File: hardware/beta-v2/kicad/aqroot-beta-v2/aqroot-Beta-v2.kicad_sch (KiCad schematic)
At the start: 0 parts

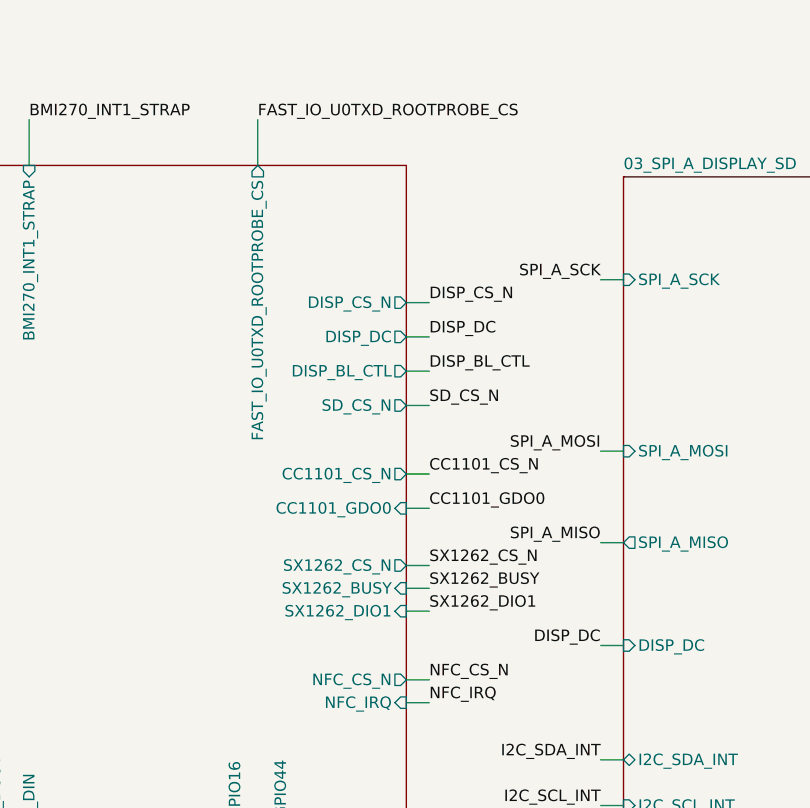
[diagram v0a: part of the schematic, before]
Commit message: hardware: migrate Full Beta v2 MCU core (FBV2-S1-002)
Closes the two power-tree values the CTO ruled on and migrates 02_MCU_CORE.
Task gate FBV2-S1-MCU-CORE = PASS. FBV2-S1 itself is 2 of 9 sheets.

P-20 - R95 680R -> 560R. Recovery recomputed from the captured circuit:
8.36 mA nominal at VBUS 5.0 V into a 0 V pack, 7.93-8.80 mA across 4.75-5.25 V,
back inside the accepted 5-10 mA band that B-26 is measured against.

The recomputation also showed that 680R was NOT arbitrary:
(5.00 - 0.32 + 4.2) / 680 = 13.06 mA is exactly B-27's recorded ~13 mA
single-fault ceiling. With 560R that ceiling becomes ~15.9 mA nominal and
~16.6 mA worst case - 0.0066 C on a 2500 mAh pack, still bounded by R95, still
unidirectional through D12, still self-annunciating. B-27 is amended in place
rather than left reading a number that is no longer true. The trade is explicit:
~21% more recovery current for ~22% more single-fault current.

P-21 - the OV trip is derived, not typed. The datasheet threshold was fetched
first (LTC4368, Farnell mirror 2243878): V_OV 492.5 / 500 / 507.5 mV rising,
hysteresis 20 / 25 / 32 mV, UV/OV leakage 10 nA max, "Adjustable +/-1.5%".
R77 4.02M -> 3.65M 1%, R78 unchanged at 442k:
0.500 x (3.65M + 442k) / 442k = 4.629 V.
Nominal 4.63 V; 4.48-4.78 V over comparator and 1% resistor tolerance;
4.44-4.82 V including worst-case OV pin leakage; release 4.40 V nominal.
Above a 4.35 V-class pack with 129 mV of worst-case margin, 420 mV below the
5.05 V first capture, and no lockout hazard because release sits above float.
3.65M is already R91's value, so this REMOVES a BOM line.

02_MCU_CORE migrated:

- GPIO38 = NATIVE_A and GPIO47 = NATIVE_B, both hierarchical and bidirectional.
  SX1262_DIO1 no longer reaches the MCU at all; under D-089 it terminates on the
  internal expander U2, which is sheet 08.
- GPIO46 = DISP_BL_CTL. GPIO46 is a strapping pin that MUST read LOW at reset -
  GPIO0 = 0 alone does not select Joint Download Boot, GPIO46 = 0 is also
  required. Three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
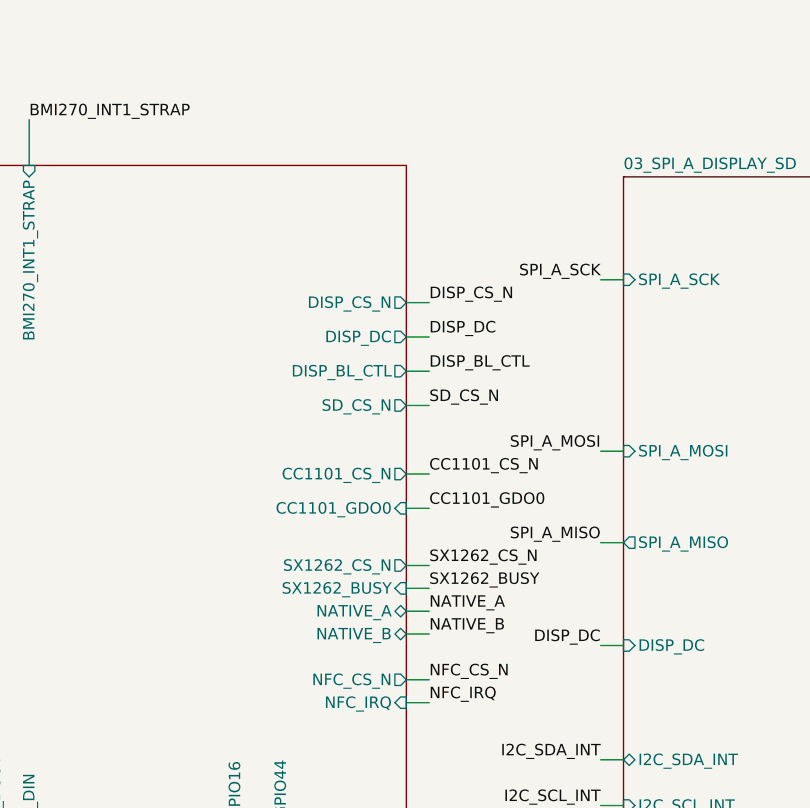
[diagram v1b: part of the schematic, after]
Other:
- sheet 02_MCU_CORE ports: added NATIVE_A, NATIVE_B; removed FAST_IO_U0TXD_ROOTPROBE_CS, SX1262_DIO1
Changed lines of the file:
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@@
 	(wire
 		(pts
-			(xy 185.42 25.4) (xy 185.42 20.32)
-		)
-		(stroke
-			(width 0)
-			(type default)
-		)
-	)
-	(wire
-		(pts
 			(xy 388.62 152.4) (xy 391.16 152.4)
 		)
@@
 	(wire
 		(pts
-			(xy 201.93 74.93) (xy 204.47 74.93)
-		)
-		(stroke
-			(width 0)
-			(type default)
-		)
-	)
-	(wire
-		(pts
 			(xy 133.35 245.11) (xy 135.89 245.11)
 		)
@@
 		)
 	)
-	(label "SX1262_DIO1"
-		(at 204.47 74.93 0)
-		(effects
-			(font
-				(size 1.27 1.27)
-			)
-			(justify left bottom)
-		)
-	)
 	(label "XGPIO0"
 		(at 391.16 132.08 0)
@@
 		)
 	)
-	(label "FAST_IO_U0TXD_ROOTPROBE_CS"
-		(at 185.42 20.32 0)
-		(effects
-			(font
-				(size 1.27 1.27)
-			)
-			(justify left bottom)
-		)
-	)
 	(label "I2C_SDA_INT"
 		(at 52.07 228.6 180)
@@
 			)
 		)
-		(pin "FAST_IO_U0TXD_ROOTPROBE_CS" output
-			(at 185.42 25.4 90)
-			(effects
-				(font
-					(size 1.27 1.27)
-				)
-				(justify right)
-			)
-		)
 		(pin "I2C_SCL_INT" output
 			(at 129.54 46.99 180)
@@
 			)
 		)
-		(pin "SX1262_DIO1" input
+		(pin "NATIVE_A" bidirectional
 			(at 201.93 74.93 0)
 			(effects
@@
 			)
 		)
+		(pin "NATIVE_B" bidirectional
+			(at 201.93 77.47 0)
+			(effects
+				(font
+					(size 1.27 1.27)
+				)
+				(justify right)
+			)
+		)
 		(pin "USB_D_MCU_N" bidirectional
 			(at 144.78 25.4 90)
@@
 		(effects
 			(font
+				(size 1.27 1.27)
+			)
+			(justify left bottom)
+		)
+	)
+	(wire
+		(pts
+			(xy 201.93 74.93) (xy 204.47 74.93)
+		)
+		(stroke
+			(width 0)
+			(type default)
+		)
+	)
+	(label "NATIVE_A"
+		(at 204.47 74.93 0)
+		(effects
+			(font
+				(size 1.27 1.27)
+			)
+			(justify left bottom)
+		)
+	)
+	(wire
+		(pts
+			(xy 201.93 77.47) (xy 204.47 77.47)
+		)
+		(stroke
+			(width 0)
+			(type default)
+		)
+	)
+	(label "NATIVE_B"
+		(at 204.47 77.47 0)
+		(effects
+			(font

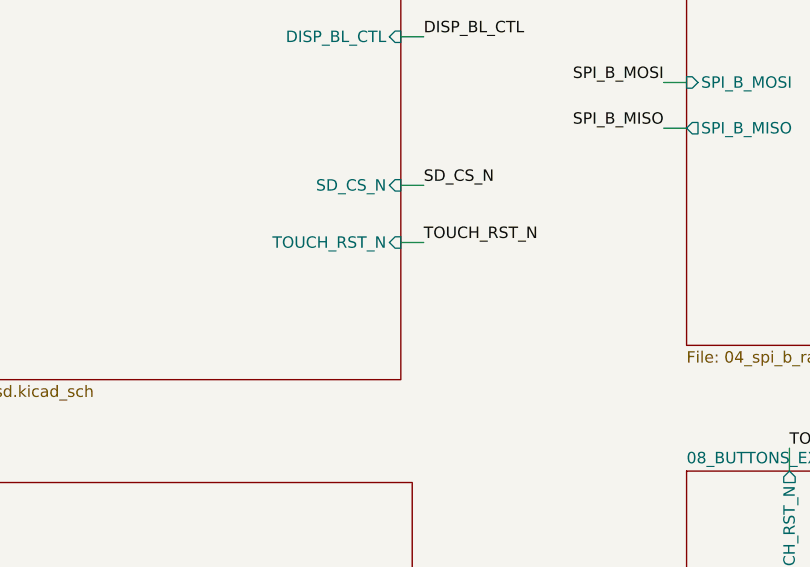
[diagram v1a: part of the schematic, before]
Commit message: hardware: migrate Full Beta v2 display and microSD (FBV2-S1-003)
Fits R111 per CTO ruling and migrates 03_SPI_A_DISPLAY_SD. Task gate
FBV2-S1-DISPLAY-SD = PASS. FBV2-S1 itself is 3 of 9 sheets.

THE INHERITED J1 WOULD HAVE PRODUCED A DEAD DISPLAY, TWICE OVER.

J1 still used the 2.8-inch CH280QV10_CT_50P pin table while its Value and
Footprint fields already read FH69-50S-0.5SH. Pin count matched, connector
matched, ERC was silent. The pin FUNCTIONS did not match ER-TFT035IPS-6:

  panel pin 1/2/3   old: LEDK / LED-A1 / LED-A2   new: LEDA / LEDK / LEDK
                    -> backlight reverse-biased, no light
  panel pin 36/37   old: WR_RS->DISP_DC / RS_SCL->SPI_A_SCK
                    new: WRX(SCL) / D-CX
                    -> clock and D/C swapped, no valid command ever reaches
                       the panel
  panel pin 4,5,6   old: LED-A3, LED-A4, IM0(grounded)   new: NC
  panel pin 7,8,9   old: IM1,IM2,IM3   new: IM0,IM1,IM2  (all three were
                    already +3V3, so 1 1 1 was correct by luck)
  panel pin 46      CTP IRQ, not represented at all

Neither fault is visible from a pin count, a connector MPN or an ERC run. A new
project-library symbol ER-TFT035IPS-6_50P was authored with the vendor table
verbatim (datasheet Rev 2.0 sec 4.1), deliberately keeping the old pin geometry
so the migration is a pin-function change and not a redraw. CH280QV10_CT_50P
stays in the library - Beta-DM still uses it - and is dropped from sheet 03's
symbol cache.

R111 FITTED (D-111). 10k, GPIO45_VDDSPI_STRAP -> GND. VDD_SPI is held LOW
deterministically instead of relying on the chip's internal pull-down alone.
TP1 retained, no capacitance on the net, no peripheral on GPIO45.

B-43 CLOSED WITH A PRIMARY SOURCE (D-116). TPS61169 datasheet SNVSA40B:
R_PD, CTRL pin internal pull-down resistor, 300 kohm, with V_H/V_L = 1.2/0.4 V
and t_SD = 2.5 ms. CTRL's only internal element pulls DOWN, so there is no
mechanism by which the backlight driver can raise the GPIO46 strap. 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
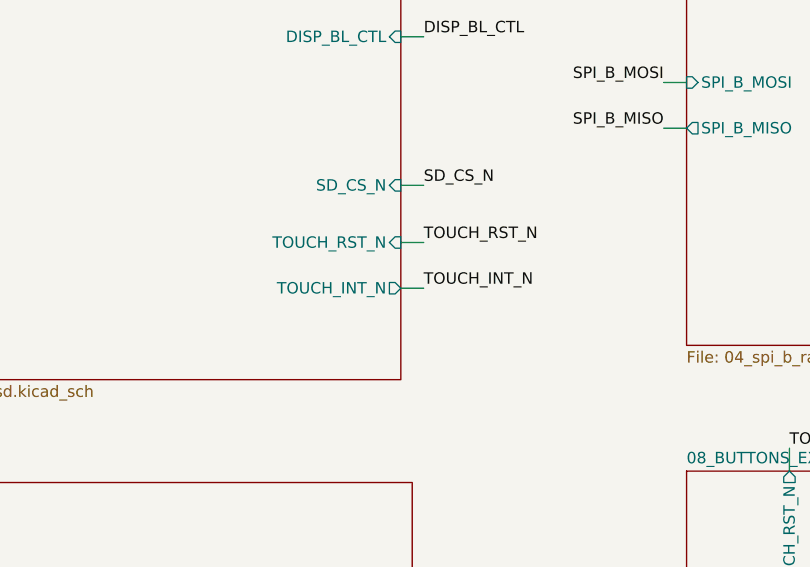
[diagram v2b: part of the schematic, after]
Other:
- sheet 03_SPI_A_DISPLAY_SD ports: added TOUCH_INT_N; removed none
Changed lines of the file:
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@@
+			)
+		)
+		(pin "TOUCH_INT_N" output
+			(at 290.83 95.25 0)
+			(effects
+				(font
+					(size 1.27 1.27)
+				)
+				(justify right)
 			)
 		)
@@
 		(effects
 			(font
+				(size 1.27 1.27)
+			)
+			(justify left bottom)
+		)
+	)
+	(wire
+		(pts
+			(xy 290.83 95.25) (xy 293.37 95.25)
+		)
+		(stroke
+			(width 0)
+			(type default)
+		)
+	)
+	(label "TOUCH_INT_N"
+		(at 293.37 95.25 0)
+		(effects
+			(font

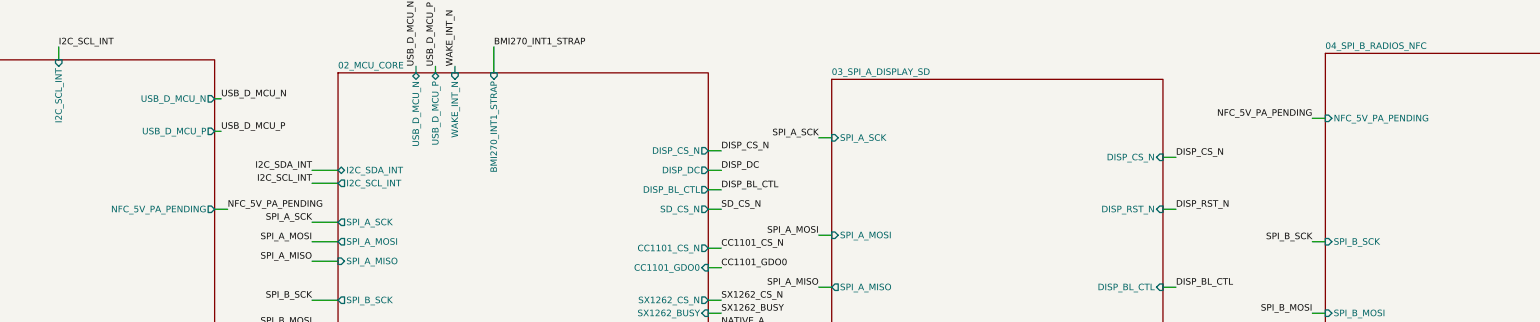
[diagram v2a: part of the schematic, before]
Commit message: hardware: migrate Full Beta v2 radios and NFC (FBV2-S1-004)
Sheet 04. Task gate FBV2-S1-RADIOS-NFC = PASS. FBV2-S1 itself is 4 of 9 sheets.

ERC: 4 errors -> 2. Total 86 -> 68. Zero added, eighteen removed. This is the
first migration task to REDUCE the project's error count, and it did so by
deleting placeholder architecture rather than by suppressing anything.

ZERO *_TBD NETS REMAIN ANYWHERE IN THE PROJECT. Sheet 04 alone retired fourteen.

RF ARCHITECTURE LOCKED (D-118).
433 MHz: INTERNAL flex. U7 IPEX -> 100 mm coax -> Taoglas FXP450.07.0100C against
a plastic wall. 915 MHz: EXTERNAL. U8 IPEX -> short pigtail -> top-panel SMA
female bulkhead, user-changeable. Neither band has a motherboard 50 ohm RF trace,
a matching network, an RF switch or a diplexer - both modules present their own
matched 50 ohm port, so the board's RF involvement at 433/915 is zero copper.
This supersedes the internal-FXP890 plan for 915 in "12 - RF and Antenna Plan".
The U7 IPEX socket must remain SERVICE-ACCESSIBLE with the shell open: if
internal 433 performance disappoints on the first units the flex unplugs and an
external pigtail replaces it with no PCB respin. That is an FBV2-P1 placement
constraint and the reason an internal antenna is an acceptable first-build risk.

433 ANTENNA VERIFIED, MATING PROVEN RATHER THAN ASSUMED (D-119). Taoglas
datasheet SPE-23-8-180-A, verbatim: "410-470MHz Flexible PCB Antenna with 100mm
1.37 IPEX MHFI". 47 x 17 x 0.28 mm, adhesive mount, gain -0.36 / -1.57 /
-0.05 dBi, Active, 54 in stock, $5.52 @ 1, MOQ 1. The antenna terminates in IPEX
MHF I and Ebyte's manual lists the E07-400M10S interface as IPEX-1 / stamp hole;
MHF I, IPEX-1 and U.FL are one mating interface, so no cable variant is needed.
Mechanical reservation recorded for FBV2-P1: plastic wall, LEFT/LOWER-SIDE, NOT
on the PCB, clear of the LiPo, the NFC loop and ferrite, the speaker magnet,
large ground pours, metal bosses, the USB shell, the 915 bulkhead/pigtail and the
IR structures.

915 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
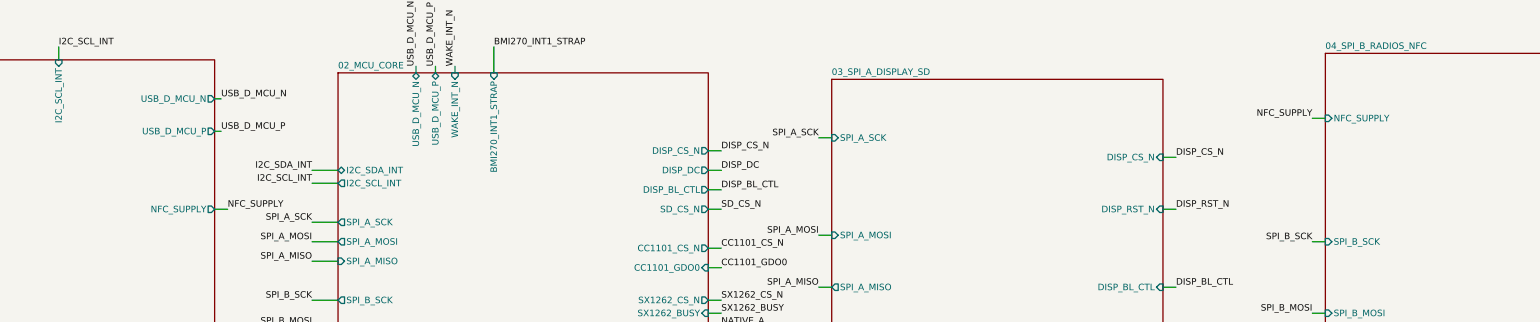
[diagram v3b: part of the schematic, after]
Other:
- sheet 01_POWER_TREE ports: added NFC_SUPPLY; removed NFC_5V_PA_PENDING
- sheet 04_SPI_B_RADIOS_NFC ports: added NFC_SUPPLY; removed NFC_5V_PA_PENDING
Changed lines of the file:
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@@
 		)
 	)
-	(label "NFC_5V_PA_PENDING"
+	(label "NFC_SUPPLY"
 		(at 107.95 52.07 0)
 		(effects
@@
 		)
 	)
-	(label "NFC_5V_PA_PENDING"
+	(label "NFC_SUPPLY"
 		(at 320.04 34.29 180)
 		(effects
@@
 			)
 		)
-		(pin "NFC_5V_PA_PENDING" input
+		(pin "NFC_SUPPLY" input
 			(at 322.58 34.29 180)
 			(effects
@@
 			)
 		)
-		(pin "NFC_5V_PA_PENDING" output
+		(pin "NFC_SUPPLY" output
 			(at 105.41 52.07 0)
 			(effects

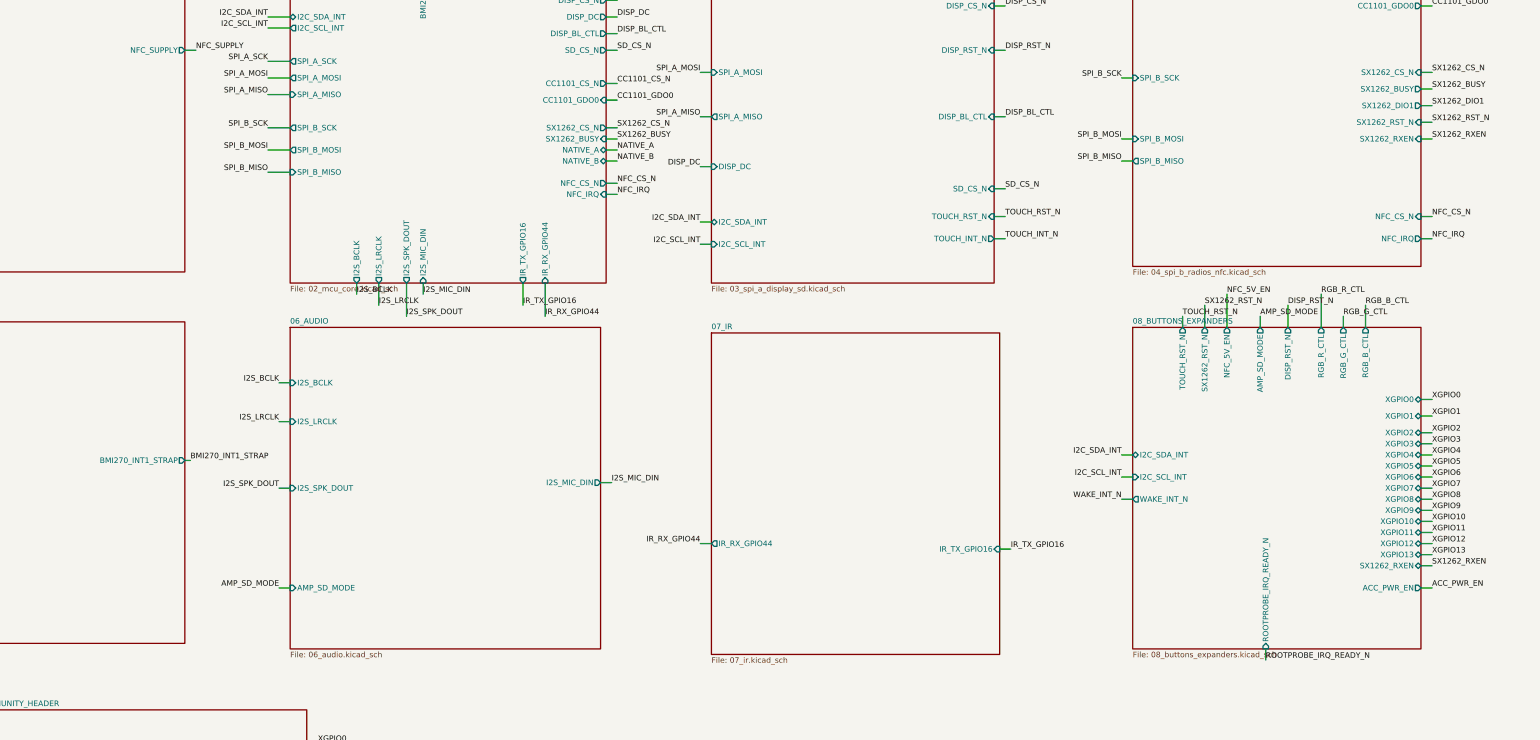
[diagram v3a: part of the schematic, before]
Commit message: hardware: migrate Full Beta v2 buttons expanders and RGB status
Sheet 08 migrated (FBV2-S1-008), resumed after a session-limit interruption.
All prior work was uncommitted working-tree change; it was inspected, kept and
finished rather than restarted.

Both expanders are NXP PCAL9535APW,118, verified against PCAL9535A Rev. 2
(23-Jan-2015) and NOT treated as a behavioural drop-in: it powers up with every
interrupt masked, the opposite of the TCA9535. U2 = 0x20, U3 = 0x21 preserved.

The two-expander allocation genuinely fails: 35 committed signals against 32
pins, with zero free native GPIO (so the WS2812 escape is impossible),
RESERVED_SPARE mandated by D-094 and ten XGPIO locked by D-082. Closed by U23,
a third PCAL9535APW,118 at 0x22 carrying only the front RGB and the reserved
spare - no new MPN, no new footprint, no new driver, no new rail, and B-37
retired with 12 spare I/O. Core, community and safety functions are placed
before the RGB by construction.

Landed: BQ25185_STAT1/STAT2 (10k pull-ups), SD_CARD_DETECT_N, TOUCH_INT_N,
SX1262_DIO1 on U2; ACC_3V3_EN, ACC_5V_EN, ACC_DETECT_N, ACC_POWER_FAULT_N on
U3. RESERVED_SPARE created on U23 P03 with R130 and TP41 - it had never existed.

Front RGB: D13 MEIHUA MHPA3528RGBCT (LCSC C409779), common anode, R124 1k /
R125 680R / R126 390R = 1.50 / 1.03 / 1.67 mA, white 4.20 mA. Dark by
construction with no external pull-ups.

IR receiver reverted to TSOP38238 (AGC2), TSOP38438 retained as a documented
drop-in fallback. Closes O-5.

Sheets 01 and 03 touched only to promote six local labels to hierarchical so
the required nets could reach the expanders; no component, value, topology or
DNP state changed.

ERC 42 messages / 1 error / 41 warnings - identical violation set to the
recovered tree and better than the 45/2/43 pre-sheet-08 baseline. Zero new
errors. fork_equivalence.py PASS, netclass_probe.py PASS, PCB still
bit-identical to Beta-DM. Sheet 09 untouched.

Co-Authored-By: Claude Opus 5 <noreply@anthropic.com>
Claud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
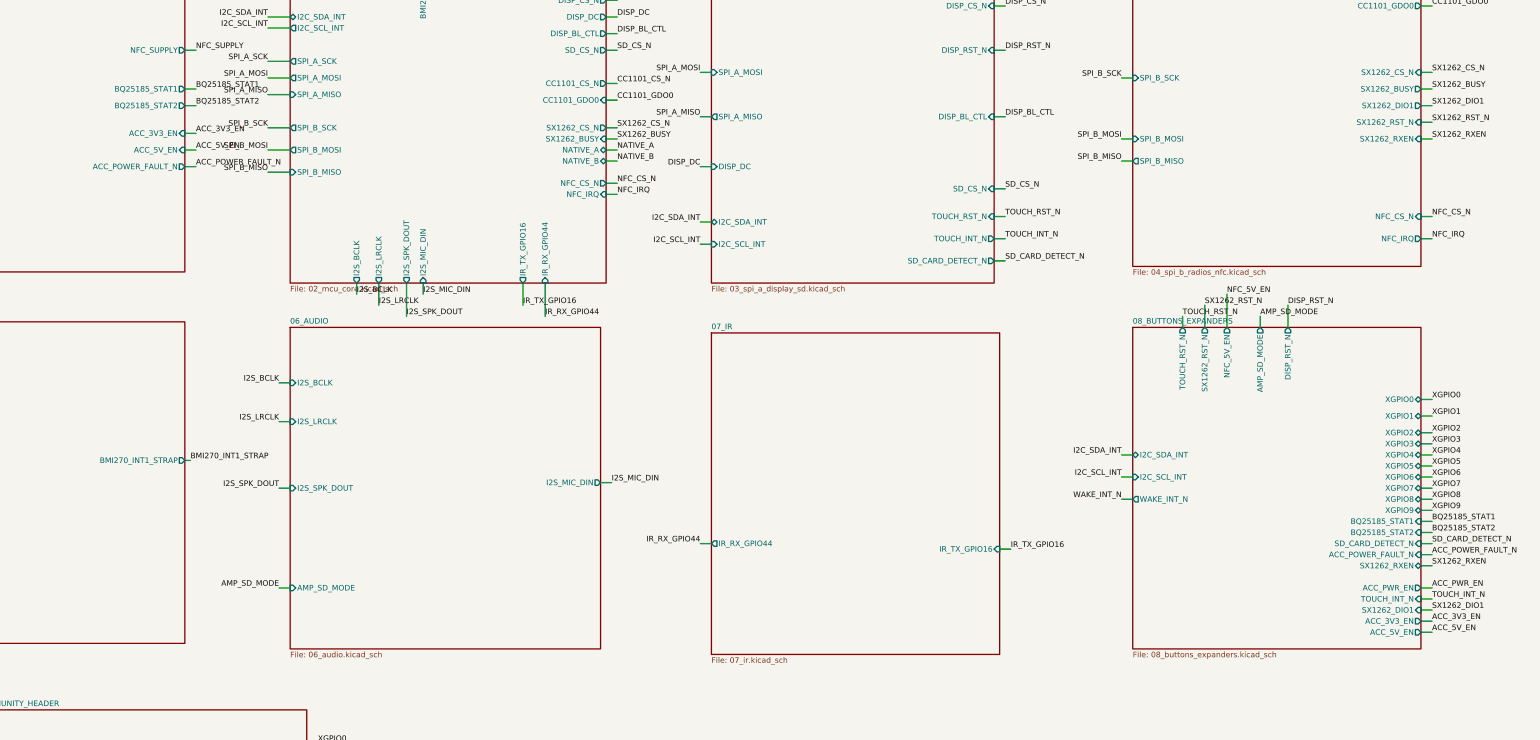
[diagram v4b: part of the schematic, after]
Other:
- sheet 01_POWER_TREE ports: added ACC_3V3_EN, ACC_5V_EN, ACC_POWER_FAULT_N, BQ25185_STAT1, BQ25185_STAT2; removed none
- sheet 03_SPI_A_DISPLAY_SD ports: added SD_CARD_DETECT_N; removed none
- sheet 08_BUTTONS_EXPANDERS ports: added ACC_3V3_EN, ACC_5V_EN, ACC_POWER_FAULT_N, BQ25185_STAT1, BQ25185_STAT2, SD_CARD_DETECT_N, SX1262_DIO1, TOUCH_INT_N; removed RGB_B_CTL, RGB_G_CTL, RGB_R_CTL, ROOTPROBE_IRQ_READY_N, XGPIO10, XGPIO11, XGPIO12, XGPIO13
